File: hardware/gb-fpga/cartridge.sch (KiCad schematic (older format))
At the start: 1 part, among them J2 Cartridge-32bit

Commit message: Rename cartridge symbol
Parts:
- removed J2: Cartridge-32bit, gb-fpga:Cartridge-DMG, symbol gb-fpga:Cartridge-32bit
- added J2: Cartridge-32pin, gb-fpga:Cartridge-DMG, symbol gb-fpga:Cartridge-32pin
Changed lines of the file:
@@
 $EndDescr
-$Comp
-L gb-fpga:Cartridge-32bit J2
-U 1 1 60D540F7
-P 5700 4000
-F 0 "J2" H 5968 4111 50  0000 L CNN
-F 1 "Cartridge-32bit" H 5968 4020 50  0000 L CNN
-F 2 "gb-fpga:Cartridge-DMG" H 5700 4550 50  0001 C CNN
-F 3 "" H 5700 4550 50  0001 C CNN
-	1    5700 4000
-	1    0    0    -1
-$EndComp
 $Comp
 L power:GND #PWR0105
@@
 Wire Wire Line
 	5500 5500 5500 5550
+$Comp
+L gb-fpga:Cartridge-32pin J2
+U 1 1 60D43C17
+P 5700 4000
+F 0 "J2" H 5968 4111 50  0000 L CNN
+F 1 "Cartridge-32pin" H 5968 4020 50  0000 L CNN
+F 2 "gb-fpga:Cartridge-DMG" H 5700 4550 50  0001 C CNN
+F 3 "" H 5700 4550 50  0001 C CNN
+	1    5700 4000
+	1    0    0    -1
+$EndComp
 $EndSCHEMATC

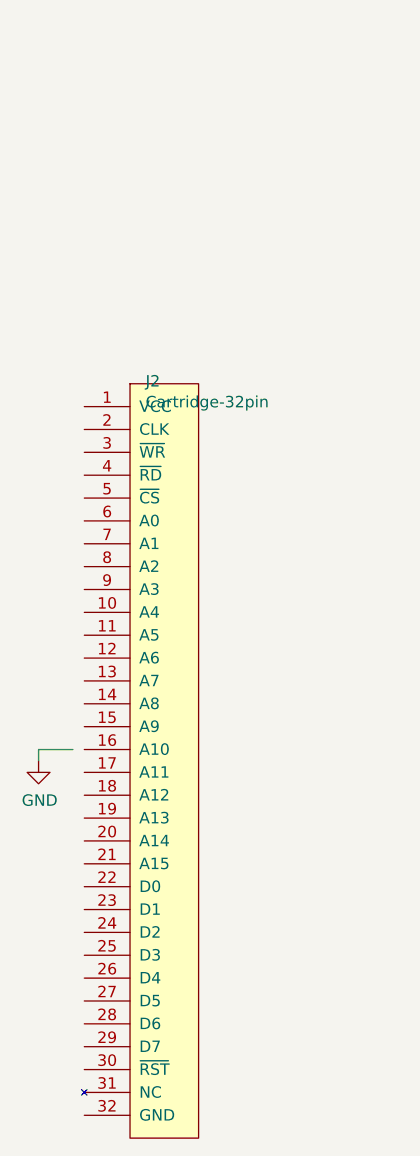
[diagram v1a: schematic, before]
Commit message: Add local fpga symbol
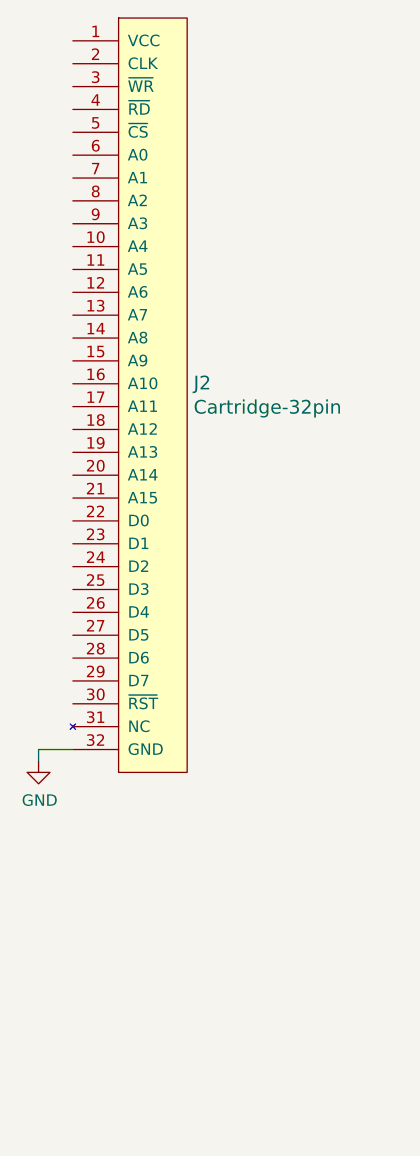
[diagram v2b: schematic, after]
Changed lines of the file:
@@
 $Comp
 L gb-fpga:Cartridge-32pin J2
-U 1 1 60D43C17
-P 5700 4000
-F 0 "J2" H 5968 4111 50  0000 L CNN
-F 1 "Cartridge-32pin" H 5968 4020 50  0000 L CNN
-F 2 "gb-fpga:Cartridge-DMG" H 5700 4550 50  0001 C CNN
-F 3 "" H 5700 4550 50  0001 C CNN
-	1    5700 4000
+U 1 1 60D4B0EF
+P 5650 2400
+F 0 "J2" H 6178 903 60  0000 L CNN
+F 1 "Cartridge-32pin" H 6178 797 60  0000 L CNN
+F 2 "gb-fpga:Cartridge-DMG" H 5850 2450 60  0001 L CNN
+F 3 "" H 5850 2250 60  0001 L CNN
+	1    5650 2400
 	1    0    0    -1
 $EndComp

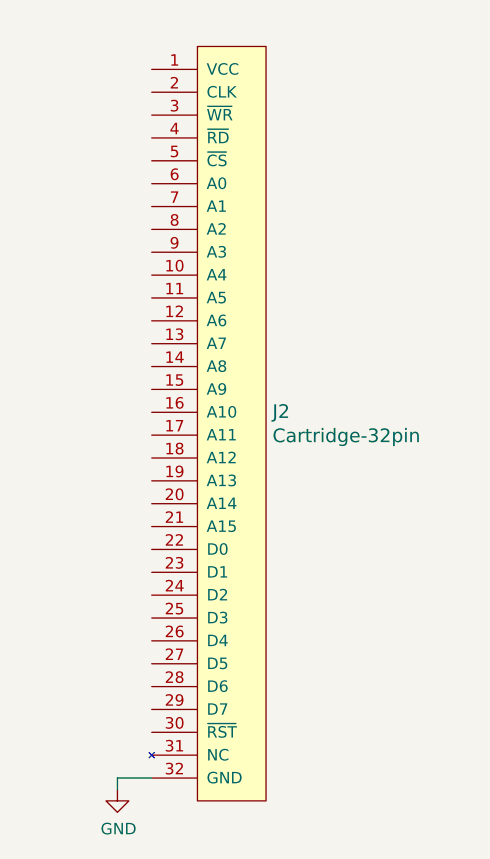
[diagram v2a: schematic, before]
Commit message: Label cartridge connections
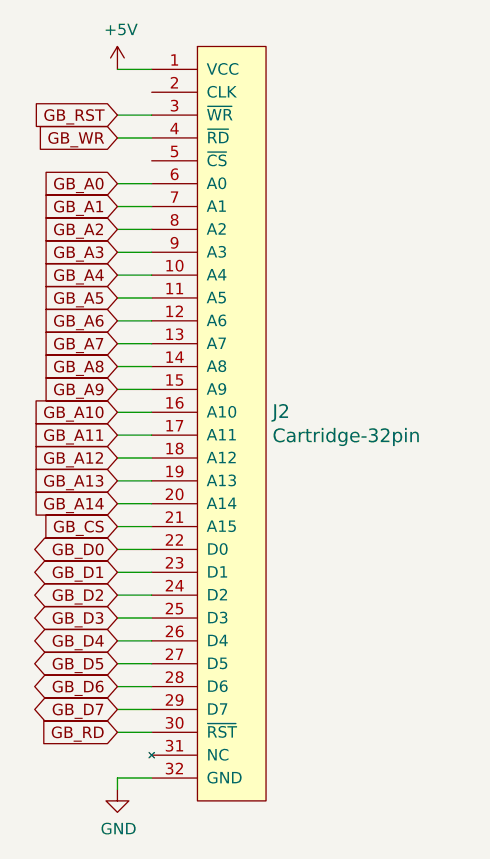
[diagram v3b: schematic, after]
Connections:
- net +5V: now reaches J2.1 (VCC)
- net GB_A4: now reaches J2.10 (A4)
- net GB_A5: now reaches J2.11 (A5)
- net GB_A6: now reaches J2.12 (A6)
- net GB_A7: now reaches J2.13 (A7)
- net GB_A8: now reaches J2.14 (A8)
- net GB_A9: now reaches J2.15 (A9)
- net GB_A10: now reaches J2.16 (A10)
- net GB_A11: now reaches J2.17 (A11)
- net GB_A12: now reaches J2.18 (A12)
- net GB_A13: now reaches J2.19 (A13)
- net GB_A14: now reaches J2.20 (A14)
- net GB_CS: now reaches J2.21 (A15)
- net GB_D0: now reaches J2.22 (D0)
- net GB_D1: now reaches J2.23 (D1)
- net GB_D2: now reaches J2.24 (D2)
- net GB_D3: now reaches J2.25 (D3)
- net GB_D4: now reaches J2.26 (D4)
- net GB_D5: now reaches J2.27 (D5)
- net GB_D6: now reaches J2.28 (D6)
- net GB_D7: now reaches J2.29 (D7)
- net GB_RST: now reaches J2.3 (~WR~)
- net GB_RD: now reaches J2.30 (~RST~)
- net GB_WR: now reaches J2.4 (~RD~)
- net GB_A0: now reaches J2.6 (A0)
- net GB_A1: now reaches J2.7 (A1)
- net GB_A2: now reaches J2.8 (A2)
- net GB_A3: now reaches J2.9 (A3)
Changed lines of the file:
@@
 $Descr A4 11693 8268
 encoding utf-8
-Sheet 6 6
+Sheet 5 6
 Title ""
 Date ""
@@
 	1    0    0    -1
 $EndComp
+$Comp
+L power:+5V #PWR?
+U 1 1 60EE2CF5
+P 5500 2400
+F 0 "#PWR?" H 5500 2250 50  0001 C CNN
+F 1 "+5V" H 5515 2573 50  0000 C CNN
+F 2 "" H 5500 2400 50  0001 C CNN
+F 3 "" H 5500 2400 50  0001 C CNN
+	1    5500 2400
+	1    0    0    -1
+$EndComp
+Wire Wire Line
+	5500 2400 5650 2400
+Text GLabel 5500 2600 0    50   Input ~ 0
+GB_RST
+Text GLabel 5500 2700 0    50   Input ~ 0
+GB_WR
+Text GLabel 5500 2900 0    50   Input ~ 0
+GB_A0
+Text GLabel 5500 3000 0    50   Input ~ 0
+GB_A1
+Text GLabel 5500 3100 0    50   Input ~ 0
+GB_A2
+Text GLabel 5500 3200 0    50   Input ~ 0
+GB_A3
+Text GLabel 5500 3300 0    50   Input ~ 0
+GB_A4
+Text GLabel 5500 3400 0    50   Input ~ 0
+GB_A5
+Text GLabel 5500 3500 0    50   Input ~ 0
+GB_A6
+Text GLabel 5500 3600 0    50   Input ~ 0
+GB_A7
+Text GLabel 5500 3700 0    50   Input ~ 0
+GB_A8
+Text GLabel 5500 3800 0    50   Input ~ 0
+GB_A9
+Text GLabel 5500 3900 0    50   Input ~ 0
+GB_A10
+Text GLabel 5500 4000 0    50   Input ~ 0
+GB_A11
+Text GLabel 5500 4100 0    50   Input ~ 0
+GB_A12
+Text GLabel 5500 4200 0    50   Input ~ 0
+GB_A13
+Text GLabel 5500 4300 0    50   Input ~ 0
+GB_A14
+Text GLabel 5500 4400 0    50   Input ~ 0
+GB_CS
+Text GLabel 5500 4500 0    50   BiDi ~ 0
+GB_D0
+Text GLabel 5500 4600 0    50   BiDi ~ 0
+GB_D1
+Text GLabel 5500 4700 0    50   BiDi ~ 0
+GB_D2
+Text GLabel 5500 4800 0    50   BiDi ~ 0
+GB_D3
+Text GLabel 5500 4900 0    50   BiDi ~ 0
+GB_D4
+Text GLabel 5500 5000 0    50   BiDi ~ 0
+GB_D5
+Text GLabel 5500 5100 0    50   BiDi ~ 0
+GB_D6
+Text GLabel 5500 5200 0    50   BiDi ~ 0
+GB_D7
+Text GLabel 5500 5300 0    50   Input ~ 0
+GB_RD
+Wire Wire Line
+	5500 2600 5650 2600
+Wire Wire Line
+	5500 2700 5650 2700
+Wire Wire Line
+	5500 2900 5650 2900
+Wire Wire Line
+	5500 3000 5650 3000
+Wire Wire Line
+	5500 3100 5650 3100
+Wire Wire Line
+	5500 3200 5650 3200
+Wire Wire Line
+	5500 3300 5650 3300
+Wire Wire Line
+	5500 3400 5650 3400
+Wire Wire Line
+	5500 3500 5650 3500
+Wire Wire Line
+	5500 3600 5650 3600
+Wire Wire Line
+	5500 3700 5650 3700
+Wire Wire Line
+	5500 3800 5650 3800
+Wire Wire Line
+	5500 3900 5650 3900
+Wire Wire Line
+	5500 4000 5650 4000
+Wire Wire Line
+	5500 4100 5650 4100
+Wire Wire Line
+	5500 4200 5650 4200
+Wire Wire Line
+	5500 4300 5650 4300
+Wire Wire Line
+	5500 4400 5650 4400
+Wire Wire Line
+	5500 4500 5650 4500
+Wire Wire Line
+	5500 4600 5650 4600
+Wire Wire Line
+	5500 4700 5650 4700
+Wire Wire Line
+	5500 4800 5650 4800
+Wire Wire Line
+	5500 4900 5650 4900
+Wire Wire Line
+	5500 5000 5650 5000
+Wire Wire Line
+	5500 5100 5650 5100
+Wire Wire Line
+	5500 5200 5650 5200
+Wire Wire Line
+	5500 5300 5650 5300
 $EndSCHEMATC

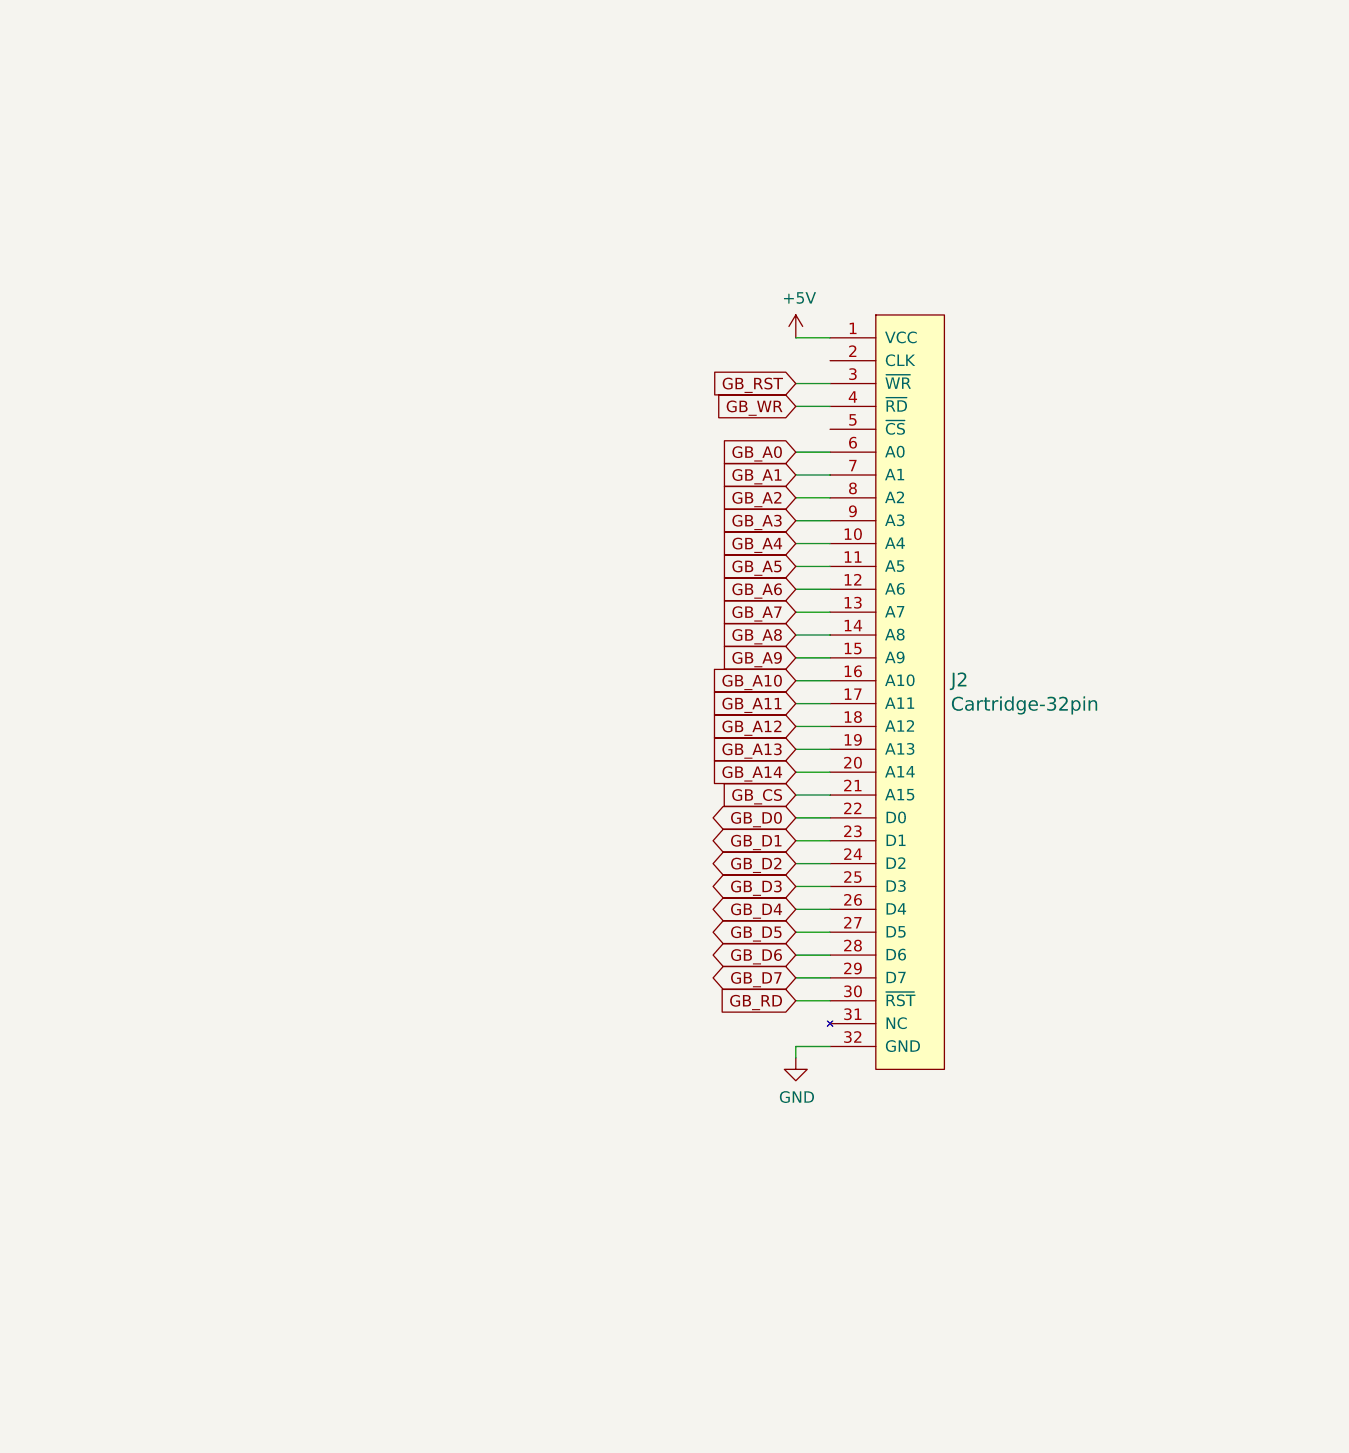
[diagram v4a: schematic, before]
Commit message: Hook up cartridge to translation ics
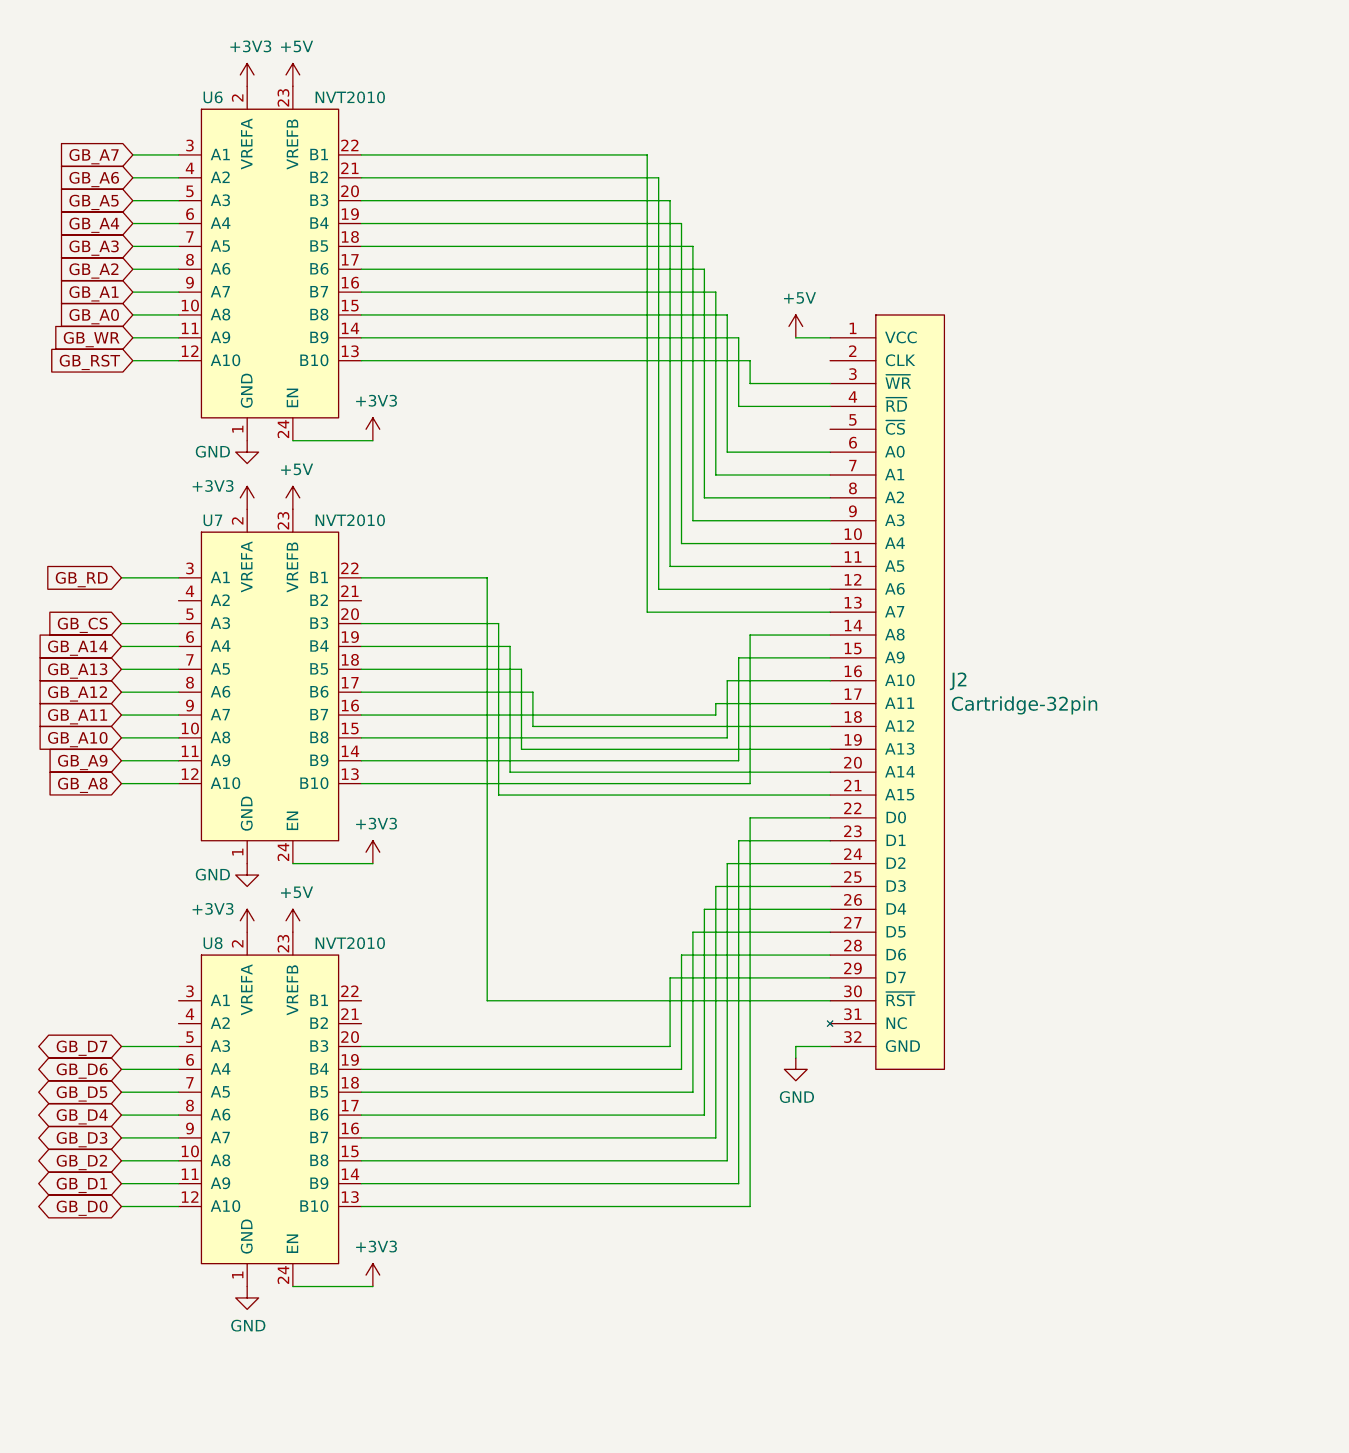
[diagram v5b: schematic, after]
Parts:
- added U6, U7, U8: NVT2010, Package_SO:TSSOP-24_4.4x7.8mm_P0.65mm, symbol Logic_LevelTranslator:NVT2010
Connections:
- net +5V: now also U6.23 (VREFB), U7.23 (VREFB), U8.23 (VREFB)
- net GB_A0: now also U6.10 (A8); no longer J2.6 (A0)
- net GB_A1: now also U6.9 (A7); no longer J2.7 (A1)
- net GB_A10: now also U7.10 (A8); no longer J2.16 (A10)
- net GB_A11: now also U7.9 (A7); no longer J2.17 (A11)
- net GB_A12: now also U7.8 (A6); no longer J2.18 (A12)
- net GB_A13: now also U7.7 (A5); no longer J2.19 (A13)
- net GB_A14: now also U7.6 (A4); no longer J2.20 (A14)
- net GB_A2: now also U6.8 (A6); no longer J2.8 (A2)
- net GB_A3: now also U6.7 (A5); no longer J2.9 (A3)
- net GB_A4: now also U6.6 (A4); no longer J2.10 (A4)
- net GB_A5: now also U6.5 (A3); no longer J2.11 (A5)
- net GB_A6: now also U6.4 (A2); no longer J2.12 (A6)
- net GB_A7: now also U6.3 (A1); no longer J2.13 (A7)
- net GB_A8: now also U7.12 (A10); no longer J2.14 (A8)
- net GB_A9: now also U7.11 (A9); no longer J2.15 (A9)
- net GB_CS: now also U7.5 (A3); no longer J2.21 (A15)
- net GB_D0: now also U8.12 (A10); no longer J2.22 (D0)
- net GB_D1: now also U8.11 (A9); no longer J2.23 (D1)
- net GB_D2: now also U8.10 (A8); no longer J2.24 (D2)
- net GB_D3: now also U8.9 (A7); no longer J2.25 (D3)
- net GB_D4: now also U8.8 (A6); no longer J2.26 (D4)
- net GB_D5: now also U8.7 (A5); no longer J2.27 (D5)
- net GB_D6: now also U8.6 (A4); no longer J2.28 (D6)
- net GB_D7: now also U8.5 (A3); no longer J2.29 (D7)
- net GB_RD: now also U7.3 (A1); no longer J2.30 (~RST~)
- net GB_RST: now also U6.12 (A10); no longer J2.3 (~WR~)
- net GB_WR: now also U6.11 (A9); no longer J2.4 (~RD~)
- net GND: now also U6.1 (GND), U7.1 (GND), U8.1 (GND)
- new net: J2.10 (A4), U6.19 (B4)
- new net: J2.11 (A5), U6.20 (B3)
- new net: J2.12 (A6), U6.21 (B2)
- new net: J2.13 (A7), U6.22 (B1)
- new net: J2.14 (A8), U7.13 (B10)
- new net: J2.15 (A9), U7.14 (B9)
- new net: J2.16 (A10), U7.15 (B8)
- new net: J2.17 (A11), U7.16 (B7)
- new net: J2.18 (A12), U7.17 (B6)
- new net: J2.19 (A13), U7.18 (B5)
- new net: J2.20 (A14), U7.19 (B4)
- new net: J2.21 (A15), U7.20 (B3)
- new net: J2.22 (D0), U8.13 (B10)
- new net: J2.23 (D1), U8.14 (B9)
- new net: J2.24 (D2), U8.15 (B8)
- new net: J2.25 (D3), U8.16 (B7)
- new net: J2.26 (D4), U8.17 (B6)
- new net: J2.27 (D5), U8.18 (B5)
- new net: J2.28 (D6), U8.19 (B4)
- new net: J2.29 (D7), U8.20 (B3)
- new net: J2.3 (~WR~), U6.13 (B10)
- new net: J2.30 (~RST~), U7.22 (B1)
- new net: J2.4 (~RD~), U6.14 (B9)
- new net: J2.6 (A0), U6.15 (B8)
- new net: J2.7 (A1), U6.16 (B7)
- new net: J2.8 (A2), U6.17 (B6)
- new net: J2.9 (A3), U6.18 (B5)
- new net +3V3: U6.2 (VREFA), U6.24 (EN), U7.2 (VREFA), U7.24 (EN), U8.2 (VREFA), U8.24 (EN)
